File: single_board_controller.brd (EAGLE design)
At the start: 168.9 x 80.3 mm, 79 parts, among them IC1 MCP3008, IC2 MCP3008, K1 AQ1AD2-3, K2 RELAY, P1 B9B-EH-A, P2 STEPPER, Q1 NPN, Q2 NPN, Q3 NPN, Q4 NPN, Q7 TRANSISTIOR, Q8 TRANSISTIOR, T1 BTA41, U1 OPTOISOLATOR-2SOIC8, U2 OPTOISOLATOR-2SOIC8, U4 OPTO-ISO

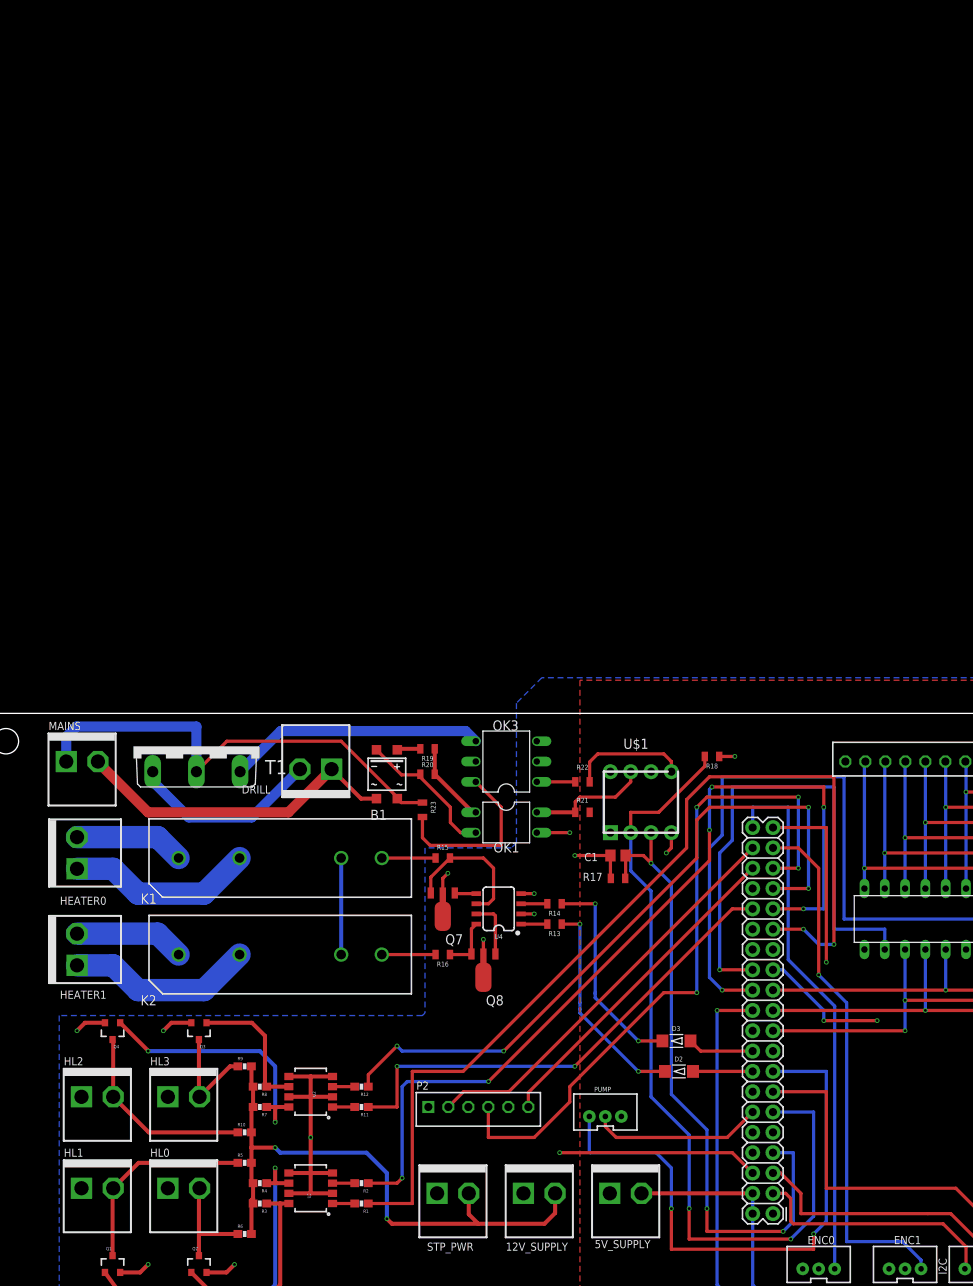
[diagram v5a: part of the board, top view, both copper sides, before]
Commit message: in process of replacing components
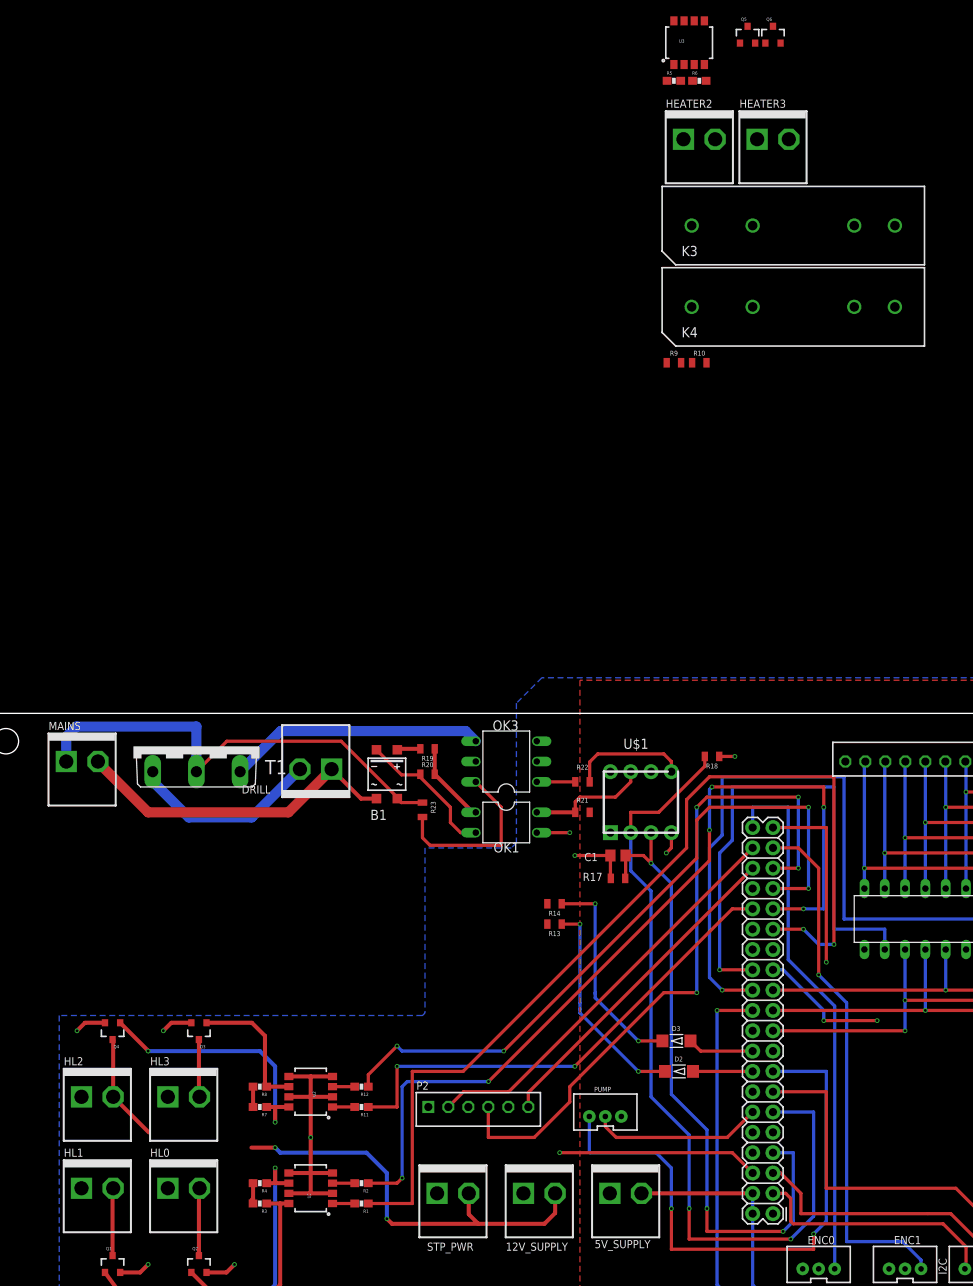
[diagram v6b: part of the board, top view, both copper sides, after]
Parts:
- removed HEATER0, HEATER1: B2P-VH, con-jst-vh:B2P-VH
- removed K1: AQ1AD2-3, relay:AQ1
- removed K2: RELAY, relay:AQ1
- removed Q7, Q8: TRANSISTIOR, semicon-smd-ipc:SOT89
- removed R15, R16: 100, SparkFun-Resistors:0805
- removed U4: OPTO-ISO, SparkFun-DiscreteSemi:SO08
- added HEATER2, HEATER3: B2P-VH, con-jst-vh:B2P-VH
- added K3: AQ1AD2-3, relay:AQ1
- added K4: RELAY, relay:AQ1
- added Q5, Q6: NPN, SparkFun-DiscreteSemi:SOT23-3
- added U3: OPTOISOLATOR-2SOIC8, SparkFun-DiscreteSemi:SO08-2
- R10, R9: value 10K -> 100; device SparkFun-Resistors:0603-RES -> SparkFun-Resistors:0805
- moved R6 154.9 mm to (86.7, 179.1)
- moved R5 145.5 mm to (83.5, 179.1)
- moved R10 111.7 mm to (86.7, 143.8)
- moved R9 103.0 mm to (83.5, 143.8)
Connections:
- removed net N$12: R13.2, U4.1
- removed net N$14: R14.2, U4.3
- removed net N$16: Q7.3, R15.1, U4.6
- removed net N$17: K1.4, R15.2
- removed net N$18: Q8.3, R16.1, U4.8
- removed net N$19: K2.4, R16.2
- removed net N$20: Q7.1, U4.5
- removed net N$21: Q8.1, U4.7
- new net N$22: R13.2, U3.1
- new net N$33: R14.2, U3.3
- new net N$34: K4.4, R10.2
- new net N$35: K3.4, R9.2
- new net N$36: Q6.3, R9.1
- new net N$37: Q5.3, R10.1
- new net OUT1N2: Q6.1, R5.1, U3.8
- new net OUT2N2: Q5.1, R6.1, U3.6
- net +5V: now also K3.3, K4.3; no longer K1.3, K2.3
- net 12V: now also HL0.1, HL1.1, HL2.1, HL3.1; no longer R10.2, R9.2
- net GND: now also Q5.2, Q6.2, U3.2, U3.4, U3.5, U3.7; no longer HL0.1, HL1.1, HL2.1, HL3.1, Q7.2, Q8.2, U4.2, U4.4
- net HV0I: now also HEATER2.2, K3.1; no longer HEATER0.2, K1.1
- net HV0O: now also HEATER2.1, K3.2; no longer HEATER0.1, K1.2
- net HV1I: now also HEATER3.2, K4.1; no longer HEATER1.2, K2.1
- net HV1O: now also HEATER3.1, K4.2; no longer HEATER1.1, K2.2
- net OUT0: now also HL1.2; no longer HL0.2, R6.1
- net OUT1: now also HL0.2; no longer HL1.2, R5.1
- net OUT2: no longer R10.1
- net OUT3: no longer R9.1
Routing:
- net HV0O: track 23.4 -> 0.00 mm
- net HV1O: track 23.4 -> 0.00 mm
- net N$16: track 17.6 -> 0.00 mm
- net OUT1: track 25.4 -> 8.35 mm
- net 12V: track 74.5 -> 58.8 mm
- net HV1I: track 13.8 -> 0.00 mm
- net HV0I: track 13.8 -> 0.00 mm
- net +5V: track 12.1 -> 0.00 mm
- net OUT2: track 24.6 -> 13.5 mm
- net GND: track 141.7 -> 133.4 mm, vias 17 -> 13
- net N$21: track 7.26 -> 0.00 mm
- net N$19: track 6.72 -> 0.00 mm
- net N$17: track 6.72 -> 0.00 mm
- net N$18: track 6.70 -> 0.00 mm
- net OUT3: track 13.6 -> 7.08 mm
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
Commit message: already sent to fab, working on small improvements
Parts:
- removed K3: AQ1AD2-3, relay:AQ1
- removed K4: RELAY, relay:AQ1
- removed Q6: NPN, SparkFun-DiscreteSemi:SOT23-3
- added -12V_SUPPLY: B2P-VH, con-jst-vh:B2P-VH
- added K1, K2: AQE12105, G6DN_relay:AQE
- added Q8: 35A/25V/8.5mΩ, SparkFun-DiscreteSemi:DPAK
- Q1, Q2, Q3, Q4, Q5: value NPN -> 35A/25V/8.5mΩ; device SparkFun-DiscreteSemi:SOT23-3 -> SparkFun-DiscreteSemi:DPAK
- moved HEATER3 138.9 mm to (2.22, 69.2), turned to 90 degrees
- moved HEATER2 125.4 mm to (2.22, 79.1), turned to 90 degrees
- moved Q5 115.7 mm to (49.5, 77.5), turned to 90 degrees
- moved R6 115.1 mm to (60.3, 67.0)
- moved U3 112.3 mm to (63.5, 73.7), turned to 90 degrees
- moved R5 101.8 mm to (60.0, 80.0)
- moved R10 89.9 mm to (36.5, 69.2), turned to 180 degrees
- moved R9 82.3 mm to (35.2, 77.2), turned to 180 degrees
- moved Q4 37.6 mm to (49.8, 69.2), turned to 90 degrees
- moved Q3 12.6 mm to (12.1, 56.8), turned to 90 degrees
- moved Q2 5.99 mm to (27.3, 26.0), turned to 90 degrees
- moved R12 5.75 mm to (45.1, 47.6)
- moved U1 5.75 mm to (38.7, 34.9)
- moved R1 5.75 mm to (45.1, 33.0)
- moved R11 5.75 mm to (45.1, 45.1)
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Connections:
- removed net HV0I: HEATER2.2, K3.1
- removed net HV0O: HEATER2.1, K3.2
- removed net HV1I: HEATER3.2, K4.1
- removed net HV1O: HEATER3.1, K4.2
- removed net N$24: B1.~2, MAINS.1, R23.2, T1.A2
- removed net N$25: B1.~1, DRILL.1, MAINS.2
- removed net N$34: K4.4, R10.2
- removed net N$35: K3.4, R9.2
- new net -12V: -12V_SUPPLY.2, STP_PWR.1
- new net MAINS-H: B1.~2, HEATER2.2, HEATER3.2, MAINS.1, R23.2, T1.A2
- new net MAINS-N: B1.~1, DRILL.1, K1.3+, K2.3+, MAINS.2
- new net N$12: HEATER2.1, K1.4-
- new net N$14: K2.I+, R10.2
- new net N$16: K1.I+, R9.2
- new net N$17: HEATER3.1, K2.4-
- new net VCC: U3.6, U3.8
- net +5V: now also K1.I-, K2.I-; no longer K3.3, K4.3
- net 12V: now also U1.6, U1.8, U2.6, U2.8; no longer R3.2, R4.2, R5.2, R6.2, R7.2, R8.2
- net GND: now also -12V_SUPPLY.1, Q1.3, Q2.3, Q3.3, Q4.3, Q5.3, Q8.3, R3.2, R4.2, R5.2, R6.2, R7.2, R8.2; no longer Q1.2, Q2.2, Q3.2, Q4.2, Q5.2, Q6.2, STP_PWR.1, U1.5, U1.7, U2.5, U2.7, U3.5, U3.7
- net N$36: now also Q5.4; no longer Q6.3
- net N$37: now also Q4.4; no longer Q5.3
- net OUT0: now also Q1.4; no longer Q2.3
- net OUT1: now also Q2.4; no longer Q1.3
- net OUT1N: now also Q1.1, U1.7; no longer Q2.1, U1.8
- net OUT1N1: now also Q3.1, U2.7; no longer Q4.1, U2.8
- net OUT1N2: now also Q5.1, U3.7; no longer Q6.1, U3.8
- net OUT2: now also Q3.4; no longer Q4.3
- net OUT2N: now also Q2.1, U1.5; no longer Q1.1, U1.6
- net OUT2N1: now also Q8.1, U2.5; no longer Q3.1, U2.6
- net OUT2N2: now also Q4.1, U3.5; no longer Q5.1, U3.6
- net OUT3: now also Q8.4; no longer Q3.3
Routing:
- net N$24: track 58.6 -> 0.00 mm
- net MAINS-H: track 0.00 -> 58.6 mm
- net 12V: track 58.8 -> 116.1 mm, vias 2 -> 0
- net N$25: track 41.3 -> 0.00 mm
- net -12V: track 0.00 -> 24.2 mm
- net GND: track 133.4 -> 157.5 mm, vias 13 -> 22
- net OUT2N: track 41.9 -> 19.7 mm
- net OUT2N2: track 0.00 -> 18.0 mm
- net N$14: track 0.00 -> 14.0 mm
- net N$16: track 0.00 -> 12.4 mm
- net OUT1N2: track 0.00 -> 12.3 mm
- net N$36: track 0.00 -> 11.9 mm
- net N$17: track 0.00 -> 11.1 mm
- net N$37: track 0.00 -> 10.8 mm
- net +5V: track 0.00 -> 9.52 mm
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- added copper zone on layer 16, net MAINS-H
- added copper zone on layer 1, net MAINS-N
- added copper zone on layer 1, net N$12
- added copper zone on layer 1, net N$17
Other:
- board text added: "-Ismael Mercier"
- board text added: "Autonomous Prospecting &"
- board text added: "Carnegie Mellon University"
- board text added: "Extraction System"
- board text added: "Single Board Controller V1.0"

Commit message: final pcb and schematic for Single board controller
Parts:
- R21: value 100 -> 100K
- moved R6 12.0 mm to (61.7, 79.0)
- moved R5 11.7 mm to (61.4, 68.4)
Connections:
- removed net +5V: K1.I-, K2.I-
- removed net VCC: U3.6, U3.8
- net 12V: now also K1.I-, K2.I-, U3.6, U3.8
- net OUT1N2: now also Q4.1; no longer Q5.1
- net OUT2N2: now also Q5.1; no longer Q4.1
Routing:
- net 12V: track 116.1 -> 190.4 mm, vias 0 -> 2
- net +5V: track 9.52 -> 0.00 mm
- net OUT2N2: track 18.0 -> 9.50 mm
- net VCC: track 4.72 -> 0.00 mm
- net GND: track 157.5 -> 156.3 mm, vias 22 -> 21
